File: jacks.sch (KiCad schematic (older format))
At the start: 71 parts, among them J1 PJ301CM, J10 PJ301BM, J11 PJ301BM, J12 PJ301BM, J13 PJ301BM, J14 PJ301BM, J15 PJ301BM, J16 PJ301BM, J17 PJ301BM, J18 PJ301BM, J19 PJ301BM, J2 PJ301CM, J20 PJ301BM, J21 PJ301BM, J22 PJ301BM, J23 PJ301BM, J24 PJ301BM, J25 PJ301BM, J26 PJ301BM, J3 PJ301BM, J4 PJ301BM, J5 PJ301BM, J6 PJ301BM, J7 PJ301BM, J8 PJ301BM, J9 PJ301BM, Q1 MMBT3904, Q2 MMBT3904, Q3 MMBT3904, Q4 MMBT3904, U1 VO0600T, U2 74LV1T34, U6 MCP6004

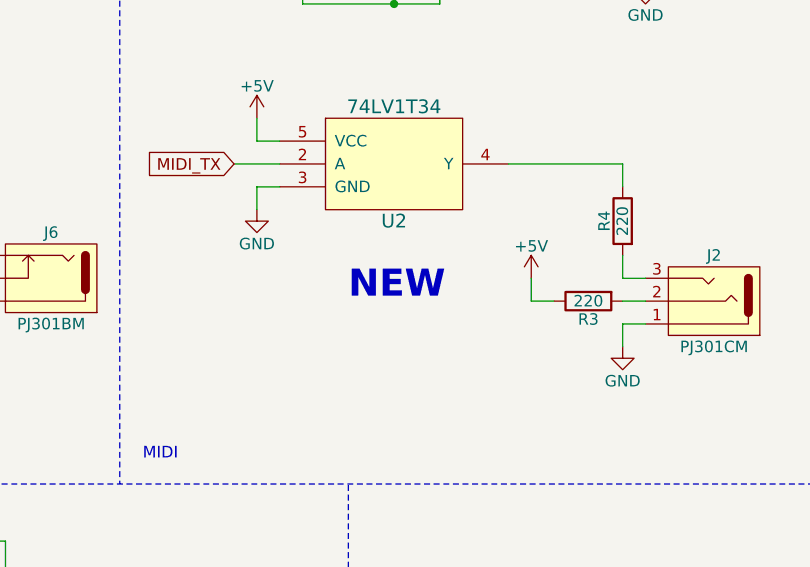
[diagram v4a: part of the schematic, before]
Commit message: cleanup schematics and updated to revision 0.3
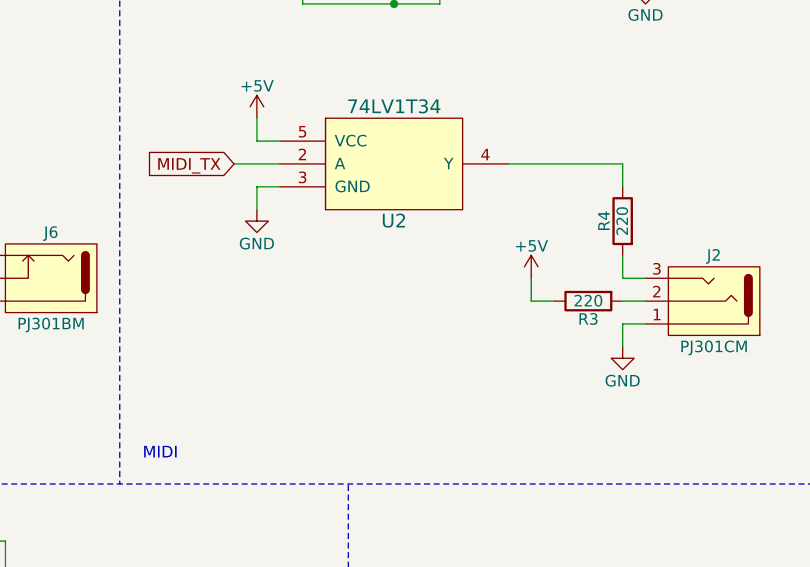
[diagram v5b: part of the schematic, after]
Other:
- note removed: "NEW"

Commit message: cleaned up schematics
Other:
- note added: "High level: 5V"
- note added: "High signal threshold: 0.7V"
- note added: "Inverting rail-to-rail opamp configuration, Input range [-5V,5V], Output range [3.3V,0V]"
- note added: "MIDI INPUT/OUTPUT"
- note removed: "MIDI"
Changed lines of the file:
@@
 Sheet 7 8
 Title "per|former eurorack sequencer"
-Date "2018-08-26"
-Rev "0.3"
+Date "2018-10-09"
+Rev "1.0"
 Comp "westlicht"
 Comment1 "cc-by-sa"
@@
 CV OUTPUTS
 Text Notes 5500 4000 0    51   ~ 0
-MIDI
+MIDI INPUT/OUTPUT
 Text Notes 2800 4000 0    51   ~ 0
 CLOCK OUTPUTS
@@
 Wire Wire Line
 	5900 5600 5900 5800
+Text Notes 1500 4000 0    51   ~ 0
+High signal threshold: 0.7V
+Text Notes 3700 4000 0    51   ~ 0
+High level: 5V
+Text Notes 1400 7600 0    51   ~ 0
+Inverting rail-to-rail opamp configuration, Input range [-5V,5V], Output range [3.3V,0V]
 $EndSCHEMATC

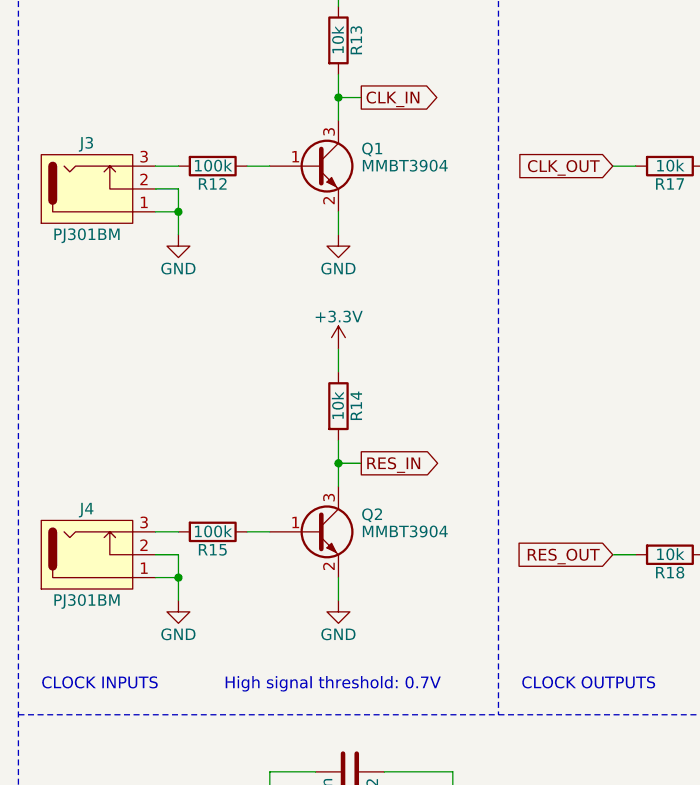
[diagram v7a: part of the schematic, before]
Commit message: revised schematic and pcb
- fixed clock/reset inputs
- schematic annotations
- moved to cc-by-nc-sa
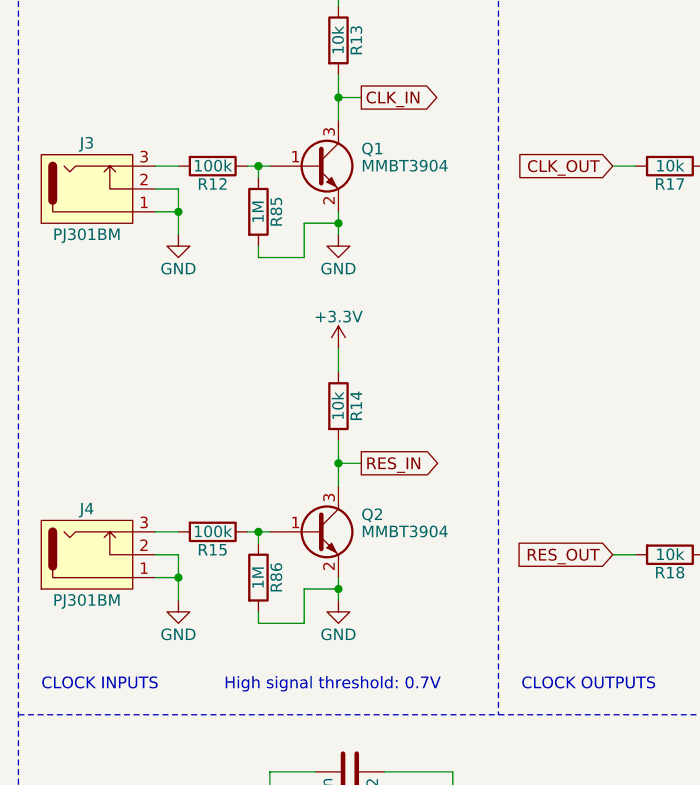
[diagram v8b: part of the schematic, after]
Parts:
- added R85, R86: 1M, w_resistor:R_0603, symbol R
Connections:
- net GND: now also R85.2, R86.2
- net at Q1.1 (B), R12.1: now also R85.1
- net at Q2.1 (B), R15.1: now also R86.1
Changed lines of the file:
@@
+	1    0    0    -1
+$EndComp
+$Comp
+L GND #PWR0116
+U 1 1 5B4BDBAA
+P 2000 4900
+F 0 "#PWR0116" H 2000 4650 50  0001 C CNN
+F 1 "GND" H 2000 4750 50  0000 C CNN
+F 2 "" H 2000 4900 50  0001 C CNN
+F 3 "" H 2000 4900 50  0001 C CNN
+	1    2000 4900
+	-1   0    0    1
+$EndComp
+$Comp
+L GND #PWR0117
+U 1 1 5B4BDC9F
+P 4400 4900
+F 0 "#PWR0117" H 4400 4650 50  0001 C CNN
+F 1 "GND" H 4400 4750 50  0000 C CNN
+F 2 "" H 4400 4900 50  0001 C CNN
+F 3 "" H 4400 4900 50  0001 C CNN
+	1    4400 4900
+	-1   0    0    1
+$EndComp
+$Comp
+L GND #PWR0118
+U 1 1 5B4BDD94
+P 2000 6400
+F 0 "#PWR0118" H 2000 6150 50  0001 C CNN
+F 1 "GND" H 2000 6250 50  0000 C CNN
+F 2 "" H 2000 6400 50  0001 C CNN
+F 3 "" H 2000 6400 50  0001 C CNN
+	1    2000 6400
+	-1   0    0    1
+$EndComp
+$Comp
+L GND #PWR0119
+U 1 1 5B4BDE89
+P 4400 6400
+F 0 "#PWR0119" H 4400 6150 50  0001 C CNN
+F 1 "GND" H 4400 6250 50  0000 C CNN
+F 2 "" H 4400 6400 50  0001 C CNN
+F 3 "" H 4400 6400 50  0001 C CNN
+	1    4400 6400
+	-1   0    0    1
+$EndComp
+$Comp
+L +3.3VA #PWR0120
+U 1 1 5B4BF3C8
+P 2000 5500
+F 0 "#PWR0120" H 2000 5350 50  0001 C CNN
+F 1 "+3.3VA" H 2000 5640 50  0000 C CNN
+F 2 "" H 2000 5500 50  0001 C CNN
+F 3 "" H 2000 5500 50  0001 C CNN
+	1    2000 5500
+	-1   0    0    1
+$EndComp
+$Comp
+L +3.3VA #PWR0121
+U 1 1 5B4BF4BD
+P 4400 5500
+F 0 "#PWR0121" H 4400 5350 50  0001 C CNN
+F 1 "+3.3VA" H 4400 5640 50  0000 C CNN
+F 2 "" H 4400 5500 50  0001 C CNN
+F 3 "" H 4400 5500 50  0001 C CNN
+	1    4400 5500
+	-1   0    0    1
+$EndComp
+$Comp
+L +3.3VA #PWR0122
+U 1 1 5B4BF80A
+P 2000 7000
+F 0 "#PWR0122" H 2000 6850 50  0001 C CNN
+F 1 "+3.3VA" H 2000 7140 50  0000 C CNN
+F 2 "" H 2000 7000 50  0001 C CNN
+F 3 "" H 2000 7000 50  0001 C CNN
+	1    2000 7000
+	-1   0    0    1
+$EndComp
+$Comp
+L +3.3VA #PWR0123
+U 1 1 5B4BF8FF
+P 4400 7000
+F 0 "#PWR0123" H 4400 6850 50  0001 C CNN
+F 1 "+3.3VA" H 4400 7140 50  0000 C CNN
+F 2 "" H 4400 7000 50  0001 C CNN
+F 3 "" H 4400 7000 50  0001 C CNN
+	1    4400 7000
+	-1   0    0    1
+$EndComp
+$Comp
+L +3.3VA #PWR0124
+U 1 1 5B4C4896
+P 5900 5100
+F 0 "#PWR0124" H 5900 4950 50  0001 C CNN
+F 1 "+3.3VA" H 5900 5240 50  0000 C CNN
+F 2 "" H 5900 5100 50  0001 C CNN
+F 3 "" H 5900 5100 50  0001 C CNN
+	1    5900 5100
+	1    0    0    -1
+$EndComp
+$Comp
+L R R85
+U 1 1 5BE63EE5
+P 1650 1900
+F 0 "R85" V 1730 1900 50  0000 C CNN
+F 1 "1M" V 1650 1900 50  0000 C CNN
+F 2 "w_resistor:R_0603" V 1580 1900 50  0001 C CNN
+F 3 "http://datasheet.octopart.com/ERJ-3EKF1004V-Panasonic-datasheet-13266541.pdf" H 1650 1900 50  0001 C CNN
+F 4 "Panasonic" H 1730 2000 50  0001 C CNN "MFN"
+F 5 "ERJ-3EKF1004V" H 1730 2000 50  0001 C CNN "MFP"
+F 6 "0603" H 1730 2000 50  0001 C CNN "Package"
+	1    1650 1900
+	1    0    0    -1
+$EndComp
+$Comp
+L R R86
+U 1 1 5BE643AF
+P 1650 3500
+F 0 "R86" V 1730 3500 50  0000 C CNN
+F 1 "1M" V 1650 3500 50  0000 C CNN
+F 2 "w_resistor:R_0603" V 1580 3500 50  0001 C CNN
+F 3 "http://datasheet.octopart.com/ERJ-3EKF1004V-Panasonic-datasheet-13266541.pdf" H 1650 3500 50  0001 C CNN
+F 4 "Panasonic" H 1730 3600 50  0001 C CNN "MFN"
+F 5 "ERJ-3EKF1004V" H 1730 3600 50  0001 C CNN "MFP"
+F 6 "0603" H 1730 3600 50  0001 C CNN "Package"
+	1    1650 3500
 	1    0    0    -1
 $EndComp
@@
 Text Notes 700  7600 0    51   ~ 0
 CV INPUTS
+Text Notes 1500 4000 0    51   ~ 0
+High signal threshold: 0.7V
+Text Notes 3700 4000 0    51   ~ 0
+High level: 5V
+Text Notes 1400 7600 0    51   ~ 0
+Inverting rail-to-rail opamp configuration, Input range [-5V,5V], Output range [3.3V,0V]
 Wire Wire Line
 	1200 1800 1300 1800
@@
 Wire Notes Line
 	6400 7700 6400 4100
+Wire Wire Line
+	5900 5100 5900 5300
+Wire Wire Line
+	5900 5600 5900 5800
+Wire Wire Line
+	1650 3350 1650 3300
+Wire Wire Line
+	1650 1750 1650 1700
+Wire Wire Line
+	1650 2100 1650 2050
+Wire Wire Line
+	1650 3700 1650 3650
+Wire Wire Line
+	1650 2100 1850 2100
+Wire Wire Line
+	1850 2100 1850 1950
+Wire Wire Line
+	1850 1950 2000 1950
+Wire Wire Line
+	1650 3700 1850 3700
+Wire Wire Line
+	1850 3700 1850 3550
+Wire Wire Line
+	1850 3550 2000 3550
 Connection ~ 1300 1900
 Connection ~ 2000 1400
@@
 Connection ~ 3700 6800
 Connection ~ 3700 5300
+Connection ~ 1650 3300
+Connection ~ 1650 1700
+Connection ~ 2000 1950
+Connection ~ 2000 3550
 NoConn ~ 8900 900
 NoConn ~ 4800 1500
@@
 NoConn ~ 7600 1550
 NoConn ~ 6100 1400
-$Comp
-L GND #PWR0116
-U 1 1 5B4BDBAA
-P 2000 4900
-F 0 "#PWR0116" H 2000 4650 50  0001 C CNN
-F 1 "GND" H 2000 4750 50  0000 C CNN
-F 2 "" H 2000 4900 50  0001 C CNN
-F 3 "" H 2000 4900 50  0001 C CNN
-	1    2000 4900
-	-1   0    0    1
-$EndComp
-$Comp
-L GND #PWR0117
-U 1 1 5B4BDC9F
-P 4400 4900
-F 0 "#PWR0117" H 4400 4650 50  0001 C CNN
-F 1 "GND" H 4400 4750 50  0000 C CNN
-F 2 "" H 4400 4900 50  0001 C CNN
-F 3 "" H 4400 4900 50  0001 C CNN
-	1    4400 4900
-	-1   0    0    1
-$EndComp
-$Comp
-L GND #PWR0118
-U 1 1 5B4BDD94
-P 2000 6400
-F 0 "#PWR0118" H 2000 6150 50  0001 C CNN
-F 1 "GND" H 2000 6250 50  0000 C CNN
-F 2 "" H 2000 6400 50  0001 C CNN
-F 3 "" H 2000 6400 50  0001 C CNN
-	1    2000 6400
-	-1   0    0    1
-$EndComp
-$Comp
-L GND #PWR0119
-U 1 1 5B4BDE89
-P 4400 6400
-F 0 "#PWR0119" H 4400 6150 50  0001 C CNN
-F 1 "GND" H 4400 6250 50  0000 C CNN
-F 2 "" H 4400 6400 50  0001 C CNN
-F 3 "" H 4400 6400 50  0001 C CNN
-	1    4400 6400
-	-1   0    0    1
-$EndComp
-$Comp
-L +3.3VA #PWR0120
-U 1 1 5B4BF3C8
-P 2000 5500
-F 0 "#PWR0120" H 2000 5350 50  0001 C CNN
-F 1 "+3.3VA" H 2000 5640 50  0000 C CNN
-F 2 "" H 2000 5500 50  0001 C CNN
-F 3 "" H 2000 5500 50  0001 C CNN
-	1    2000 5500
-	-1   0    0    1
-$EndComp
-$Comp
-L +3.3VA #PWR0121
-U 1 1 5B4BF4BD
-P 4400 5500
-F 0 "#PWR0121" H 4400 5350 50  0001 C CNN
-F 1 "+3.3VA" H 4400 5640 50  0000 C CNN
-F 2 "" H 4400 5500 50  0001 C CNN
-F 3 "" H 4400 5500 50  0001 C CNN
-	1    4400 5500
-	-1   0    0    1
-$EndComp
-$Comp
-L +3.3VA #PWR0122
-U 1 1 5B4BF80A
-P 2000 7000
-F 0 "#PWR0122" H 2000 6850 50  0001 C CNN
-F 1 "+3.3VA" H 2000 7140 50  0000 C CNN
-F 2 "" H 2000 7000 50  0001 C CNN
-F 3 "" H 2000 7000 50  0001 C CNN
-	1    2000 7000
-	-1   0    0    1
-$EndComp
-$Comp
-L +3.3VA #PWR0123
-U 1 1 5B4BF8FF
-P 4400 7000
-F 0 "#PWR0123" H 4400 6850 50  0001 C CNN
-F 1 "+3.3VA" H 4400 7140 50  0000 C CNN
-F 2 "" H 4400 7000 50  0001 C CNN
-F 3 "" H 4400 7000 50  0001 C CNN
-	1    4400 7000
-	-1   0    0    1
-$EndComp
-$Comp
-L +3.3VA #PWR0124
-U 1 1 5B4C4896
-P 5900 5100
-F 0 "#PWR0124" H 5900 4950 50  0001 C CNN
-F 1 "+3.3VA" H 5900 5240 50  0000 C CNN
-F 2 "" H 5900 5100 50  0001 C CNN
-F 3 "" H 5900 5100 50  0001 C CNN
-	1    5900 5100
-	1    0    0    -1
-$EndComp
-Wire Wire Line
-	5900 5100 5900 5300
-Wire Wire Line
-	5900 5600 5900 5800
-Text Notes 1500 4000 0    51   ~ 0
-High signal threshold: 0.7V
-Text Notes 3700 4000 0    51   ~ 0
-High level: 5V
-Text Notes 1400 7600 0    51   ~ 0
-Inverting rail-to-rail opamp configuration, Input range [-5V,5V], Output range [3.3V,0V]
 $EndSCHEMATC
